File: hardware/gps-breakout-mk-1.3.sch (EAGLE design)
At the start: 10 parts

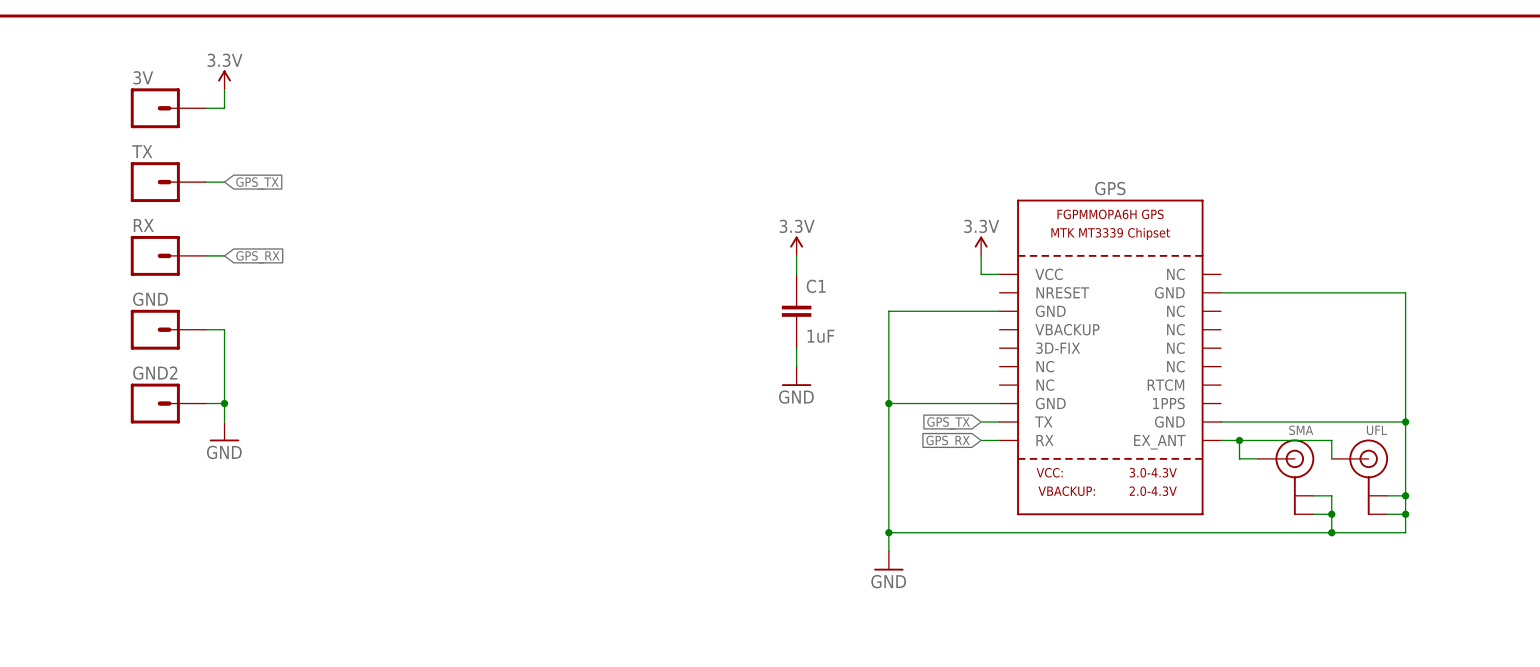
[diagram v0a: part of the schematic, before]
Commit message: change to gps module again: the rest of it
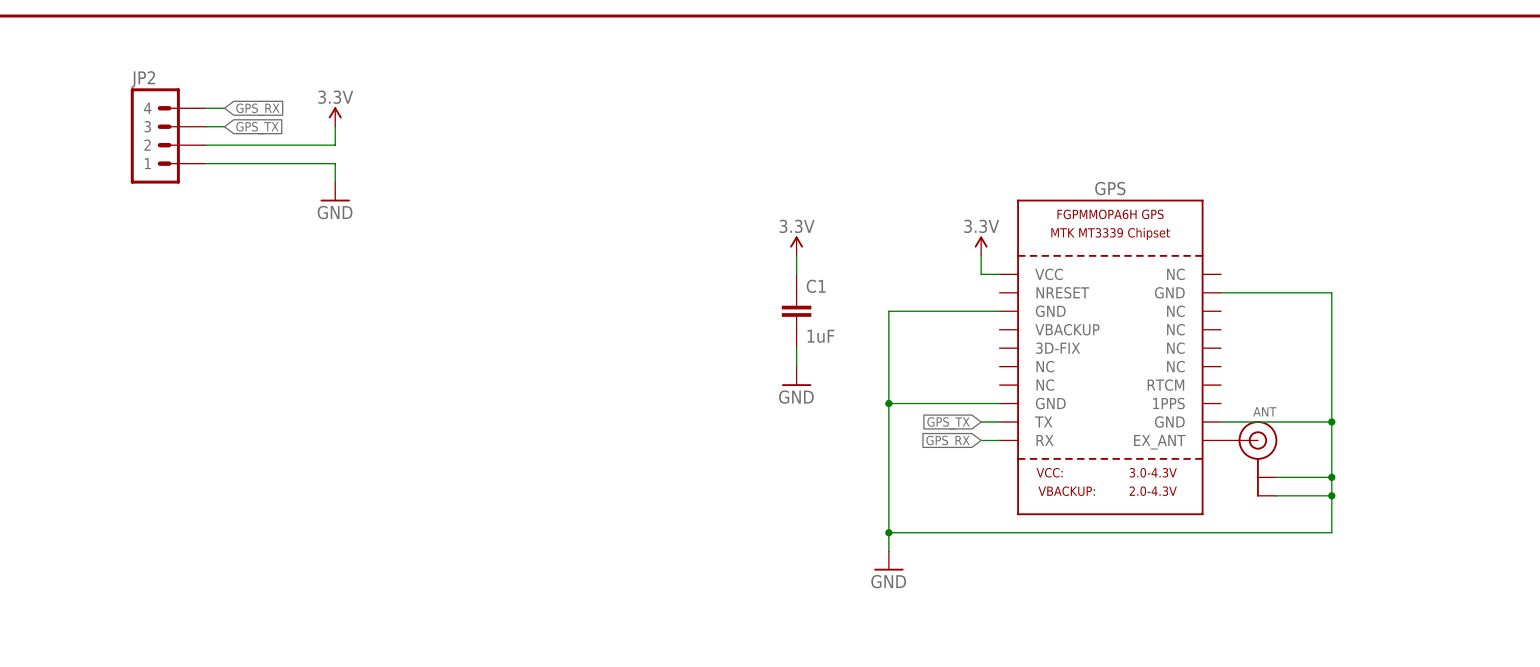
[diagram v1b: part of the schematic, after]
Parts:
- removed 3V, GND, GND2, RX, TX: M01PTH-1MM, a_parts:M01PTH-1MM
- removed SMA: (no value), a_parts:ANTENNASMA_EDGE
- removed UFL: (no value), a_parts:ANTENNAUFL
- added ANT: (no value), a_parts:ANTENNAUFL
- added JP2: M04SMD-FEMALE, a_parts:M04SMD-FEMALE
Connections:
- net 3.3V: now also JP2.2; no longer 3V.1
- net GND: now also ANT.GND@0, ANT.GND@1, JP2.1; no longer GND.1, GND2.1, SMA.GND@0, SMA.GND@1, UFL.GND@0, UFL.GND@1
- net GPS_RX: now also JP2.4; no longer RX.1
- net GPS_TX: now also JP2.3; no longer TX.1
- net N$1: now also ANT.SIGNAL; no longer SMA.SIGNAL, UFL.SIGNAL
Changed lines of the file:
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@@
 <part name="SUPPLY1" library="a_parts" deviceset="3.3V" device=""/>
 <part name="GND1" library="a_parts" deviceset="GND" device=""/>
-<part name="GND" library="a_parts" deviceset="M01" device="PTH-1MM"/>
-<part name="3V" library="a_parts" deviceset="M01" device="PTH-1MM"/>
-<part name="TX" library="a_parts" deviceset="M01" device="PTH-1MM"/>
-<part name="RX" library="a_parts" deviceset="M01" device="PTH-1MM"/>
-<part name="UFL" library="a_parts" deviceset="ANTENNA" device="UFL"/>
-<part name="GND2" library="a_parts" deviceset="M01" device="PTH-1MM"/>
-<part name="SMA" library="a_parts" deviceset="ANTENNA" device="SMA_EDGE"/>
+<part name="ANT" library="a_parts" deviceset="ANTENNA" device="UFL"/>
+<part name="JP2" library="a_parts" deviceset="M04" device="SMD-FEMALE" value="M04SMD-FEMALE"/>
 </parts>
 <sheets>
@@
 <instance part="SUPPLY7" gate="G$1" x="119.38" y="152.4"/>
 <instance part="GND8" gate="1" x="119.38" y="134.62"/>
-<instance part="SUPPLY1" gate="G$1" x="40.64" y="175.26"/>
-<instance part="GND1" gate="1" x="40.64" y="127"/>
-<instance part="GND" gate="G$1" x="30.48" y="142.24"/>
-<instance part="3V" gate="G$1" x="30.48" y="172.72"/>
-<instance part="TX" gate="G$1" x="30.48" y="162.56"/>
-<instance part="RX" gate="G$1" x="30.48" y="152.4"/>
-<instance part="UFL" gate="G$1" x="198.12" y="124.46" rot="MR0"/>
-<instance part="GND2" gate="G$1" x="30.48" y="132.08"/>
-<instance part="SMA" gate="G$1" x="187.96" y="124.46" rot="MR0"/>
+<instance part="SUPPLY1" gate="G$1" x="55.88" y="170.18"/>
+<instance part="GND1" gate="1" x="55.88" y="160.02"/>
+<instance part="ANT" gate="G$1" x="182.88" y="127" rot="MR0"/>
+<instance part="JP2" gate="G$1" x="33.02" y="167.64"/>
 </instances>
 <busses>
@@
 <junction x="132.08" y="132.08"/>
 <pinref part="GPS" gate="G$1" pin="GND@3"/>
-<wire x1="177.8" y1="129.54" x2="203.2" y2="129.54" width="0.1524" layer="91"/>
-<wire x1="203.2" y1="129.54" x2="203.2" y2="119.38" width="0.1524" layer="91"/>
+<wire x1="177.8" y1="129.54" x2="193.04" y2="129.54" width="0.1524" layer="91"/>
+<wire x1="193.04" y1="129.54" x2="193.04" y2="121.92" width="0.1524" layer="91"/>
 <pinref part="GPS" gate="G$1" pin="GND@4"/>
-<wire x1="203.2" y1="119.38" x2="203.2" y2="116.84" width="0.1524" layer="91"/>
-<wire x1="203.2" y1="116.84" x2="203.2" y2="114.3" width="0.1524" layer="91"/>
-<wire x1="177.8" y1="147.32" x2="203.2" y2="147.32" width="0.1524" layer="91"/>
-<wire x1="203.2" y1="147.32" x2="203.2" y2="129.54" width="0.1524" layer="91"/>
-<junction x="203.2" y="129.54"/>
+<wire x1="193.04" y1="121.92" x2="193.04" y2="119.38" width="0.1524" layer="91"/>
+<wire x1="193.04" y1="119.38" x2="193.04" y2="114.3" width="0.1524" layer="91"/>
+<wire x1="177.8" y1="147.32" x2="193.04" y2="147.32" width="0.1524" layer="91"/>
+<wire x1="193.04" y1="147.32" x2="193.04" y2="129.54" width="0.1524" layer="91"/>
+<junction x="193.04" y="129.54"/>
 <wire x1="132.08" y1="114.3" x2="193.04" y2="114.3" width="0.1524" layer="91"/>
 <junction x="132.08" y="114.3"/>
-<pinref part="UFL" gate="G$1" pin="GND@0"/>
-<wire x1="193.04" y1="114.3" x2="203.2" y2="114.3" width="0.1524" layer="91"/>
-<wire x1="200.66" y1="119.38" x2="203.2" y2="119.38" width="0.1524" layer="91"/>
-<junction x="203.2" y="119.38"/>
-<pinref part="UFL" gate="G$1" pin="GND@1"/>
-<wire x1="200.66" y1="116.84" x2="203.2" y2="116.84" width="0.1524" layer="91"/>
-<junction x="203.2" y="116.84"/>
-<pinref part="SMA" gate="G$1" pin="GND@0"/>
-<wire x1="190.5" y1="119.38" x2="193.04" y2="119.38" width="0.1524" layer="91"/>
-<wire x1="193.04" y1="119.38" x2="193.04" y2="116.84" width="0.1524" layer="91"/>
-<junction x="193.04" y="114.3"/>
-<pinref part="SMA" gate="G$1" pin="GND@1"/>
-<wire x1="193.04" y1="116.84" x2="193.04" y2="114.3" width="0.1524" layer="91"/>
-<wire x1="190.5" y1="116.84" x2="193.04" y2="116.84" width="0.1524" layer="91"/>
-<junction x="193.04" y="116.84"/>
+<pinref part="ANT" gate="G$1" pin="GND@0"/>
+<wire x1="185.42" y1="121.92" x2="193.04" y2="121.92" width="0.1524" layer="91"/>
+<junction x="193.04" y="121.92"/>
+<pinref part="ANT" gate="G$1" pin="GND@1"/>
+<wire x1="185.42" y1="119.38" x2="193.04" y2="119.38" width="0.1524" layer="91"/>
+<junction x="193.04" y="119.38"/>
 </segment>
 <segment>
@@
 </segment>
 <segment>
-<wire x1="38.1" y1="142.24" x2="40.64" y2="142.24" width="0.1524" layer="91"/>
+<wire x1="38.1" y1="165.1" x2="55.88" y2="165.1" width="0.1524" layer="91"/>
 <pinref part="GND1" gate="1" pin="GND"/>
-<wire x1="40.64" y1="142.24" x2="40.64" y2="132.08" width="0.1524" layer="91"/>
-<pinref part="GND" gate="G$1" pin="1"/>
-<pinref part="GND2" gate="G$1" pin="1"/>
-<wire x1="40.64" y1="132.08" x2="40.64" y2="129.54" width="0.1524" layer="91"/>
-<wire x1="38.1" y1="132.08" x2="40.64" y2="132.08" width="0.1524" layer="91"/>
-<junction x="40.64" y="132.08"/>
+<wire x1="55.88" y1="165.1" x2="55.88" y2="162.56" width="0.1524" layer="91"/>
+<pinref part="JP2" gate="G$1" pin="1"/>
 </segment>
 </net>
@@
 </segment>
 <segment>
-<wire x1="38.1" y1="172.72" x2="40.64" y2="172.72" width="0.1524" layer="91"/>
+<wire x1="38.1" y1="167.64" x2="55.88" y2="167.64" width="0.1524" layer="91"/>
 <pinref part="SUPPLY1" gate="G$1" pin="3.3V"/>
-<wire x1="40.64" y1="172.72" x2="40.64" y2="175.26" width="0.1524" layer="91"/>
-<pinref part="3V" gate="G$1" pin="1"/>
+<wire x1="55.88" y1="167.64" x2="55.88" y2="170.18" width="0.1524" layer="91"/>
+<pinref part="JP2" gate="G$1" pin="2"/>
 </segment>
 </net>
@@
 </segment>
 <segment>
-<wire x1="40.64" y1="162.56" x2="38.1" y2="162.56" width="0.1524" layer="91"/>
-<label x="40.64" y="162.56" size="1.27" layer="95" rot="MR180" xref="yes"/>
-<pinref part="TX" gate="G$1" pin="1"/>
+<wire x1="40.64" y1="170.18" x2="38.1" y2="170.18" width="0.1524" layer="91"/>
+<label x="40.64" y="170.18" size="1.27" layer="95" rot="MR180" xref="yes"/>
+<pinref part="JP2" gate="G$1" pin="3"/>
 </segment>
 </net>
@@
 </segment>
 <segment>
-<wire x1="40.64" y1="152.4" x2="38.1" y2="152.4" width="0.1524" layer="91"/>
-<label x="40.64" y="152.4" size="1.27" layer="95" rot="MR180" xref="yes"/>
-<pinref part="RX" gate="G$1" pin="1"/>
+<wire x1="40.64" y1="172.72" x2="38.1" y2="172.72" width="0.1524" layer="91"/>
+<label x="40.64" y="172.72" size="1.27" layer="95" rot="MR180" xref="yes"/>
+<pinref part="JP2" gate="G$1" pin="4"/>
 </segment>
 </net>
@@
 <segment>
 <pinref part="GPS" gate="G$1" pin="EX_ANT"/>
-<pinref part="SMA" gate="G$1" pin="SIGNAL"/>
-<wire x1="182.88" y1="124.46" x2="180.34" y2="124.46" width="0.1524" layer="91"/>
-<wire x1="180.34" y1="124.46" x2="180.34" y2="127" width="0.1524" layer="91"/>
-<wire x1="180.34" y1="127" x2="177.8" y2="127" width="0.1524" layer="91"/>
-<wire x1="180.34" y1="127" x2="193.04" y2="127" width="0.1524" layer="91"/>
-<junction x="180.34" y="127"/>
-<pinref part="UFL" gate="G$1" pin="SIGNAL"/>
-<wire x1="193.04" y1="127" x2="193.04" y2="124.46" width="0.1524" layer="91"/>
+<pinref part="ANT" gate="G$1" pin="SIGNAL"/>
 </segment>
 </net>
